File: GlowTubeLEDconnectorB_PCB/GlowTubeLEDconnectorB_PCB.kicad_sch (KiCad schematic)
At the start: 2 parts

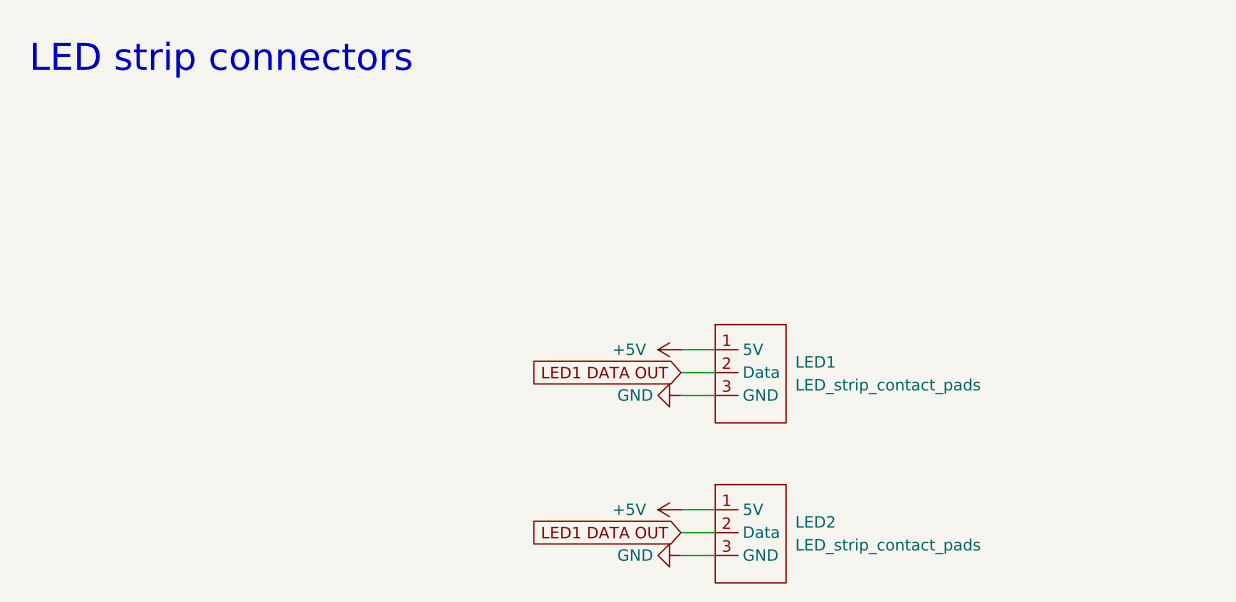
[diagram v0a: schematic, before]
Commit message: added readme to pcb files
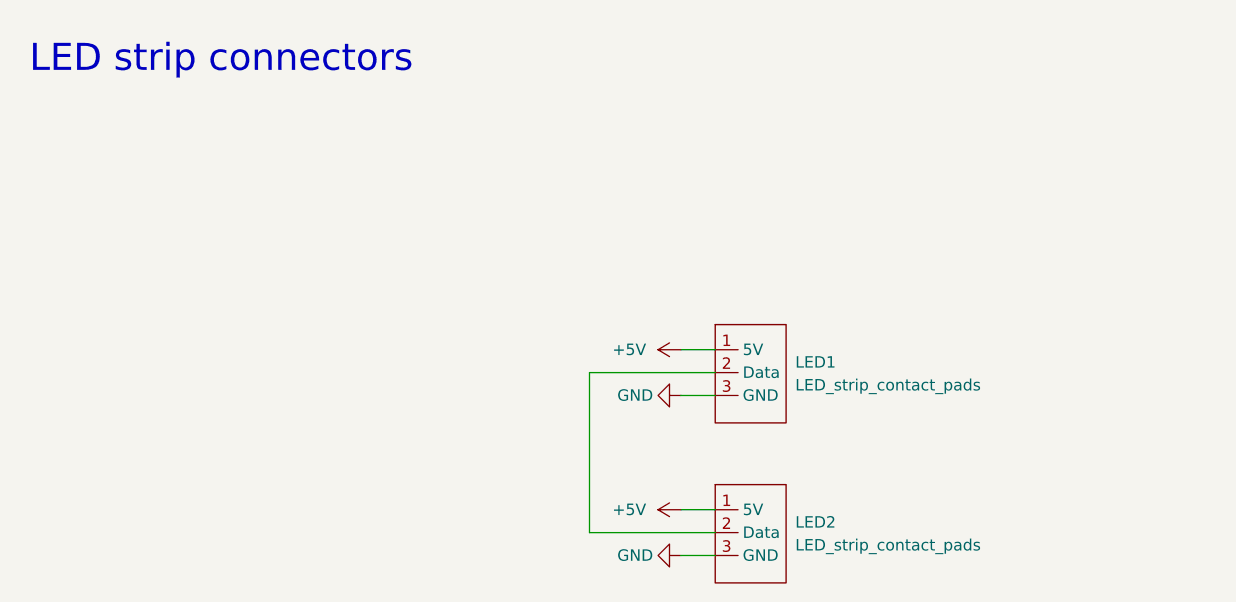
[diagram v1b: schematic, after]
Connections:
- net LED1 DATA OUT: no longer names the net of LED1.2 (Data), LED2.2 (Data)
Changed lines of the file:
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@@
+    (stroke (width 0) (type default) (color 0 0 0 0))
+  )
+  (wire (pts (xy 83.82 77.47) (xy 97.79 77.47))
     (stroke (width 0) (type default) (color 0 0 0 0))
   )
@@
     (stroke (width 0) (type default) (color 0 0 0 0))
   )
-  (wire (pts (xy 93.98 59.69) (xy 97.79 59.69))
+  (wire (pts (xy 83.82 59.69) (xy 97.79 59.69))
     (stroke (width 0) (type default) (color 0 0 0 0))
   )
-  (wire (pts (xy 93.98 77.47) (xy 97.79 77.47))
+  (wire (pts (xy 83.82 59.69) (xy 83.82 77.47))
     (stroke (width 0) (type default) (color 0 0 0 0))
   )
@@
     (effects (font (size 3 3)) (justify left bottom))
   )
-  (global_label "LED1 DATA OUT" (shape input) (at 93.98 59.69 180) (fields_autoplaced)
-    (effects (font (size 1.27 1.27)) (justify right))
-    (property "Intersheet References" "${INTERSHEET_REFS}" (id 0) (at 76.9317 59.6106 0)
-      (effects (font (size 1.27 1.27)) (justify right) hide)
-    )
-  )
-  (global_label "LED1 DATA OUT" (shape input) (at 93.98 77.47 180) (fields_autoplaced)
-    (effects (font (size 1.27 1.27)) (justify right))
-    (property "Intersheet References" "${INTERSHEET_REFS}" (id 0) (at 76.9317 77.3906 0)
-      (effects (font (size 1.27 1.27)) (justify right) hide)
-    )
-  )
   (symbol (lib_id "power:+5V") (at 93.98 57.15 90) (unit 1)

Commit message: redesigned GlowTube PCBs
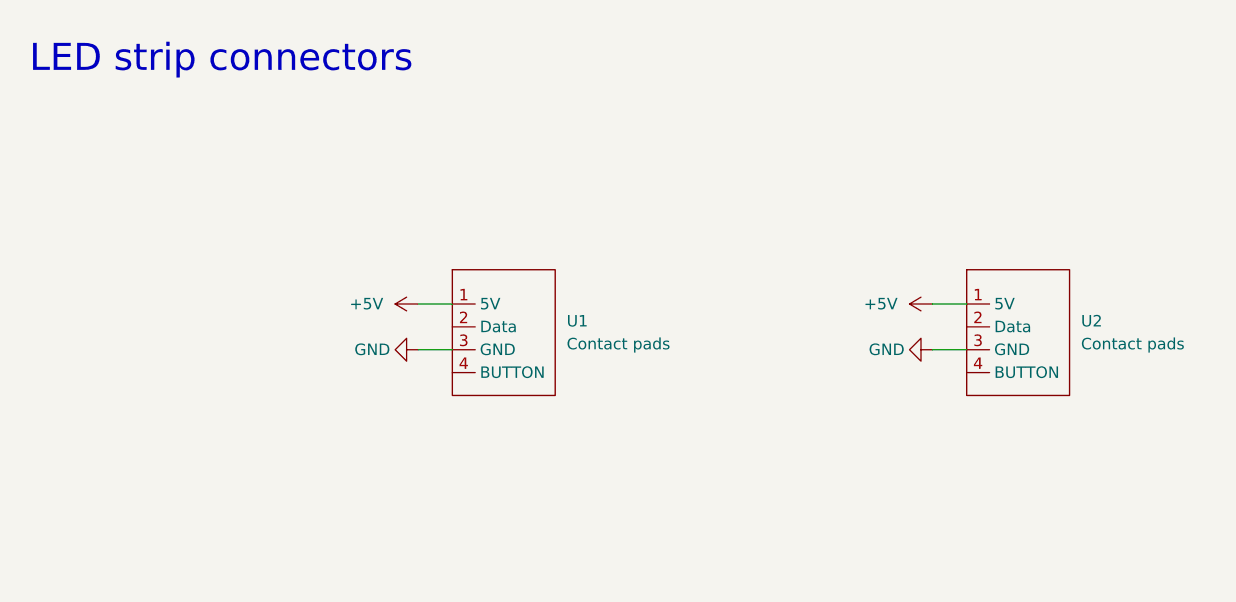
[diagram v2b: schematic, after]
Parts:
- removed LED1, LED2: LED_strip_contact_pads, Connector:LED strip connector pad, symbol Connector:LED_strip_contact_pads
- added U1, U2: Contact pads, myparts:LED strip connector 4pad small, symbol myparts:LED_strip_contact_4pads
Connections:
- net +5V: now also U1.1 (5V), U2.1 (5V)
- net GND: now also U1.3 (GND), U2.3 (GND)
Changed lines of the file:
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@@
 (kicad_sch (version 20211123) (generator eeschema)
   (paper "A5")
-  (wire (pts (xy 93.98 80.01) (xy 97.79 80.01))
+  (wire (pts (xy 64.77 52.07) (xy 68.58 52.07))
     (stroke (width 0) (type default) (color 0 0 0 0))
   )
-  (wire (pts (xy 83.82 77.47) (xy 97.79 77.47))
+  (wire (pts (xy 121.92 57.15) (xy 125.73 57.15))
     (stroke (width 0) (type default) (color 0 0 0 0))
   )
-  (wire (pts (xy 93.98 62.23) (xy 97.79 62.23))
+  (wire (pts (xy 121.92 52.07) (xy 125.73 52.07))
     (stroke (width 0) (type default) (color 0 0 0 0))
   )
-  (wire (pts (xy 83.82 59.69) (xy 97.79 59.69))
-    (stroke (width 0) (type default) (color 0 0 0 0))
-  )
-  (wire (pts (xy 83.82 59.69) (xy 83.82 77.47))
-    (stroke (width 0) (type default) (color 0 0 0 0))
-  )
-  (wire (pts (xy 93.98 57.15) (xy 97.79 57.15))
-    (stroke (width 0) (type default) (color 0 0 0 0))
-  )
-  (wire (pts (xy 93.98 74.93) (xy 97.79 74.93))
+  (wire (pts (xy 64.77 57.15) (xy 68.58 57.15))
     (stroke (width 0) (type default) (color 0 0 0 0))
   )
@@
     (effects (font (size 3 3)) (justify left bottom))
   )
-  (symbol (lib_id "power:+5V") (at 93.98 57.15 90) (unit 1)
-    (in_bom yes) (on_board yes)
-    (property "Reference" "#PWR0104" (id 0) (at 97.79 57.15 0)
+  (symbol (lib_id "myparts:LED_strip_contact_4pads") (at 72.39 52.07 0) (unit 1)
+    (in_bom yes) (on_board yes) (fields_autoplaced)
+    (property "Reference" "U1" (id 0) (at 81.28 53.9749 0)
+      (effects (font (size 1.27 1.27)) (justify left))
+    )
+    (property "Value" "Contact pads" (id 1) (at 81.28 56.5149 0)
+      (effects (font (size 1.27 1.27)) (justify left))
+    )
+    (property "Footprint" "myparts:LED strip connector 4pad small" (id 2) (at 72.39 52.07 0)
       (effects (font (size 1.27 1.27)) hide)
     )
-    (property "Value" "+5V" (id 1) (at 86.36 57.15 90)
-      (effects (font (size 1.27 1.27)) (justify right))
-    )
-    (property "Footprint" "" (id 2) (at 93.98 57.15 0)
-      (effects (font (size 1.27 1.27)) hide)
-    )
-    (property "Datasheet" "" (id 3) (at 93.98 57.15 0)
-      (effects (font (size 1.27 1.27)) hide)
-    )
-    (pin "1")
-  )
-  (symbol (lib_id "power:+5V") (at 93.98 74.93 90) (unit 1)
-    (in_bom yes) (on_board yes)
-    (property "Reference" "#PWR0102" (id 0) (at 97.79 74.93 0)
-      (effects (font (size 1.27 1.27)) hide)
-    )
-    (property "Value" "+5V" (id 1) (at 86.36 74.93 90)
-      (effects (font (size 1.27 1.27)) (justify right))
-    )
-    (property "Footprint" "" (id 2) (at 93.98 74.93 0)
-      (effects (font (size 1.27 1.27)) hide)
-    )
-    (property "Datasheet" "" (id 3) (at 93.98 74.93 0)
-      (effects (font (size 1.27 1.27)) hide)
-    )
-    (pin "1")
-  )
-  (symbol (lib_id "power:GND") (at 93.98 80.01 270) (unit 1)
-    (in_bom yes) (on_board yes)
-    (property "Reference" "#PWR0101" (id 0) (at 87.63 80.01 0)
-      (effects (font (size 1.27 1.27)) hide)
-    )
-    (property "Value" "GND" (id 1) (at 88.9 80.01 90))
-    (property "Footprint" "" (id 2) (at 93.98 80.01 0)
-      (effects (font (size 1.27 1.27)) hide)
-    )
-    (property "Datasheet" "" (id 3) (at 93.98 80.01 0)
-      (effects (font (size 1.27 1.27)) hide)
-    )
-    (pin "1")
-  )
-  (symbol (lib_id "Connector:LED_strip_contact_pads") (at 101.6 57.15 0) (unit 1)
-    (in_bom yes) (on_board yes) (fields_autoplaced)
-    (property "Reference" "LED1" (id 0) (at 106.68 58.5469 0)
-      (effects (font (size 1.27 1.27)) (justify left))
-    )
-    (property "Value" "LED_strip_contact_pads" (id 1) (at 106.68 61.0869 0)
-      (effects (font (size 1.27 1.27)) (justify left))
-    )
-    (property "Footprint" "Connector:LED strip connector pad" (id 2) (at 101.6 57.15 0)
-      (effects (font (size 1.27 1.27)) hide)
-    )
-    (property "Datasheet" "" (id 3) (at 101.6 57.15 0)
+    (property "Datasheet" "" (id 3) (at 72.39 52.07 0)
       (effects (font (size 1.27 1.27)) hide)
     )
@@
     (pin "2")
     (pin "3")
+    (pin "4")
   )
-  (symbol (lib_id "Connector:LED_strip_contact_pads") (at 101.6 74.93 0) (unit 1)
+  (symbol (lib_id "power:GND") (at 121.92 57.15 270) (unit 1)
+    (in_bom yes) (on_board yes)
+    (property "Reference" "#PWR0103" (id 0) (at 115.57 57.15 0)
+      (effects (font (size 1.27 1.27)) hide)
+    )
+    (property "Value" "GND" (id 1) (at 116.84 57.15 90))
+    (property "Footprint" "" (id 2) (at 121.92 57.15 0)
+      (effects (font (size 1.27 1.27)) hide)
+    )
+    (property "Datasheet" "" (id 3) (at 121.92 57.15 0)
+      (effects (font (size 1.27 1.27)) hide)
+    )
+    (pin "1")
+  )
+  (symbol (lib_id "power:+5V") (at 121.92 52.07 90) (unit 1)
+    (in_bom yes) (on_board yes)
+    (property "Reference" "#PWR0104" (id 0) (at 125.73 52.07 0)
+      (effects (font (size 1.27 1.27)) hide)
+    )
+    (property "Value" "+5V" (id 1) (at 114.3 52.07 90)
+      (effects (font (size 1.27 1.27)) (justify right))
+    )
+    (property "Footprint" "" (id 2) (at 121.92 52.07 0)
+      (effects (font (size 1.27 1.27)) hide)
+    )
+    (property "Datasheet" "" (id 3) (at 121.92 52.07 0)
+      (effects (font (size 1.27 1.27)) hide)
+    )
+    (pin "1")
+  )
+  (symbol (lib_id "myparts:LED_strip_contact_4pads") (at 129.54 52.07 0) (unit 1)
     (in_bom yes) (on_board yes) (fields_autoplaced)
-    (property "Reference" "LED2" (id 0) (at 106.68 76.3269 0)
+    (property "Reference" "U2" (id 0) (at 138.43 53.9749 0)
       (effects (font (size 1.27 1.27)) (justify left))
     )
-    (property "Value" "LED_strip_contact_pads" (id 1) (at 106.68 78.8669 0)
+    (property "Value" "Contact pads" (id 1) (at 138.43 56.5149 0)
       (effects (font (size 1.27 1.27)) (justify left))
     )
-    (property "Footprint" "Connector:LED strip connector pad" (id 2) (at 101.6 74.93 0)
+    (property "Footprint" "myparts:LED strip connector 4pad small" (id 2) (at 129.54 52.07 0)
       (effects (font (size 1.27 1.27)) hide)
     )
-    (property "Datasheet" "" (id 3) (at 101.6 74.93 0)
+    (property "Datasheet" "" (id 3) (at 129.54 52.07 0)
       (effects (font (size 1.27 1.27)) hide)
     )
@@
     (pin "2")
     (pin "3")
+    (pin "4")
   )
-  (symbol (lib_id "power:GND") (at 93.98 62.23 270) (unit 1)
+  (symbol (lib_id "power:GND") (at 64.77 57.15 270) (unit 1)
     (in_bom yes) (on_board yes)
-    (property "Reference" "#PWR0103" (id 0) (at 87.63 62.23 0)
+    (property "Reference" "#PWR0102" (id 0) (at 58.42 57.15 0)
       (effects (font (size 1.27 1.27)) hide)
     )
-    (property "Value" "GND" (id 1) (at 88.9 62.23 90))
-    (property "Footprint" "" (id 2) (at 93.98 62.23 0)
+    (property "Value" "GND" (id 1) (at 59.69 57.15 90))
+    (property "Footprint" "" (id 2) (at 64.77 57.15 0)
       (effects (font (size 1.27 1.27)) hide)
     )
-    (property "Datasheet" "" (id 3) (at 93.98 62.23 0)
+    (property "Datasheet" "" (id 3) (at 64.77 57.15 0)
+      (effects (font (size 1.27 1.27)) hide)
+    )
+    (pin "1")
+  )
+  (symbol (lib_id "power:+5V") (at 64.77 52.07 90) (unit 1)
+    (in_bom yes) (on_board yes)
+    (property "Reference" "#PWR0101" (id 0) (at 68.58 52.07 0)
+      (effects (font (size 1.27 1.27)) hide)
+    )
+    (property "Value" "+5V" (id 1) (at 57.15 52.07 90)
+      (effects (font (size 1.27 1.27)) (justify right))
+    )
+    (property "Footprint" "" (id 2) (at 64.77 52.07 0)
+      (effects (font (size 1.27 1.27)) hide)
+    )
+    (property "Datasheet" "" (id 3) (at 64.77 52.07 0)
       (effects (font (size 1.27 1.27)) hide)
     )
@@
   )
   (symbol_instances
-    (path "/ae3a27cf-da63-458b-b615-ef55e99a0994"
-      (reference "#PWR0101") (unit 1) (value "GND") (footprint "")
+    (path "/c9ee3dd9-b781-4e37-aefd-ea0162e13fee"
+      (reference "#PWR0101") (unit 1) (value "+5V") (footprint "")
     )
-    (path "/66c4ed0c-5a0d-4610-9403-a68378c2eab9"
-      (reference "#PWR0102") (unit 1) (value "+5V") (footprint "")
+    (path "/b3fc5d4e-0d72-4e38-8486-702804543c74"
+      (reference "#PWR0102") (unit 1) (value "GND") (footprint "")
     )
-    (path "/efa87fa3-7f38-445c-9591-962f652580f6"
+    (path "/427aa5e2-f8f3-482d-ae22-86b30e39a465"
       (reference "#PWR0103") (unit 1) (value "GND") (footprint "")
     )
-    (path "/4f3c48b9-ed3b-4e5f-b20a-218fbc7560ce"
+    (path "/506627be-637b-4014-9c50-e157b466aea8"
       (reference "#PWR0104") (unit 1) (value "+5V") (footprint "")
     )
-    (path "/e0723ce8-0ee3-4ef8-8070-26417d03176c"
-      (reference "LED1") (unit 1) (value "LED_strip_contact_pads") (footprint "Connector:LED strip connector pad")
+    (path "/1568ce5d-1305-4d2b-9586-590d6a1deb78"
+      (reference "U1") (unit 1) (value "Contact pads") (footprint "myparts:LED strip connector 4pad small")
     )
-    (path "/eb859bd5-cb67-40bf-81dc-6bcf74142183"
-      (reference "LED2") (unit 1) (value "LED_strip_contact_pads") (footprint "Connector:LED strip connector pad")
+    (path "/9107d9e2-ba91-4f39-8d0e-2d90c6554128"
+      (reference "U2") (unit 1) (value "Contact pads") (footprint "myparts:LED strip connector 4pad small")
     )
   )
